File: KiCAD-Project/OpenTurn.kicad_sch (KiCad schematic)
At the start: 5 parts

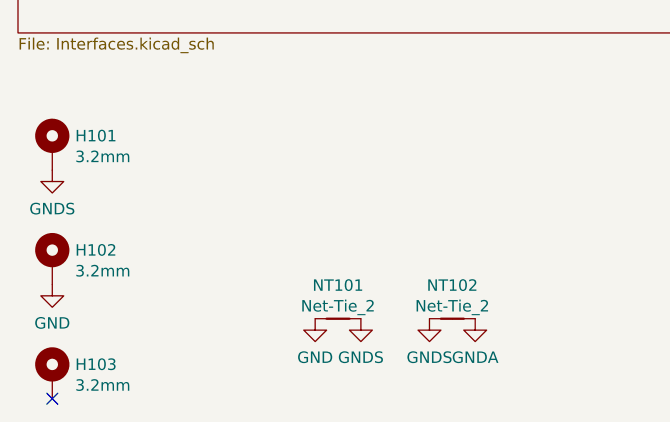
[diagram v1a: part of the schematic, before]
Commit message: DRC resolved
removed GNDA, GNDS from schematic due to no solution was found to get a net-tie in inner layers
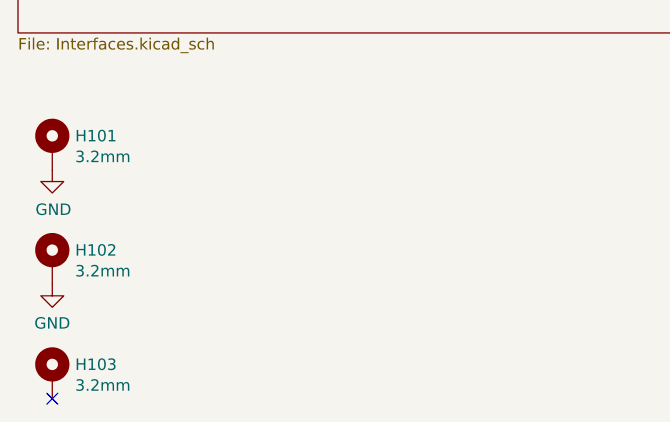
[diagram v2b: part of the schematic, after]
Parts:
- removed NT101, NT102: Net-Tie_2, NetTie:NetTie-2_SMD_Pad0.5mm, symbol Device:Net-Tie_2
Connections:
- net GNDS is gone; now on net GND: H101.1

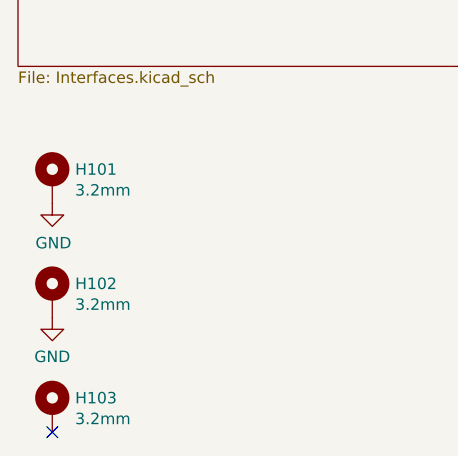
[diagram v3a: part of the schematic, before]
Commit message: changed connectors to THT
changed connectors to THT, removed UART connector
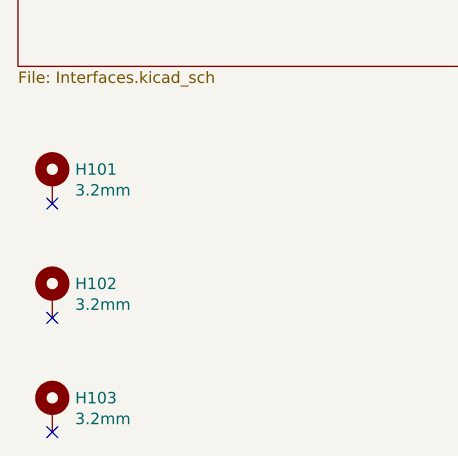
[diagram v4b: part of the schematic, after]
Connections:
- net GND: no longer names the net of H101.1
- net GND: no longer H102.1
- no-connect marks 1 -> 3
